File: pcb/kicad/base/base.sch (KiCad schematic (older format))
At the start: 34 parts, among them P1 J-Link SWD, P2 SMA, P3 Power Source, U1 SAMB11G18A-edit, Y1 32.768kHz, Y2 26MHz

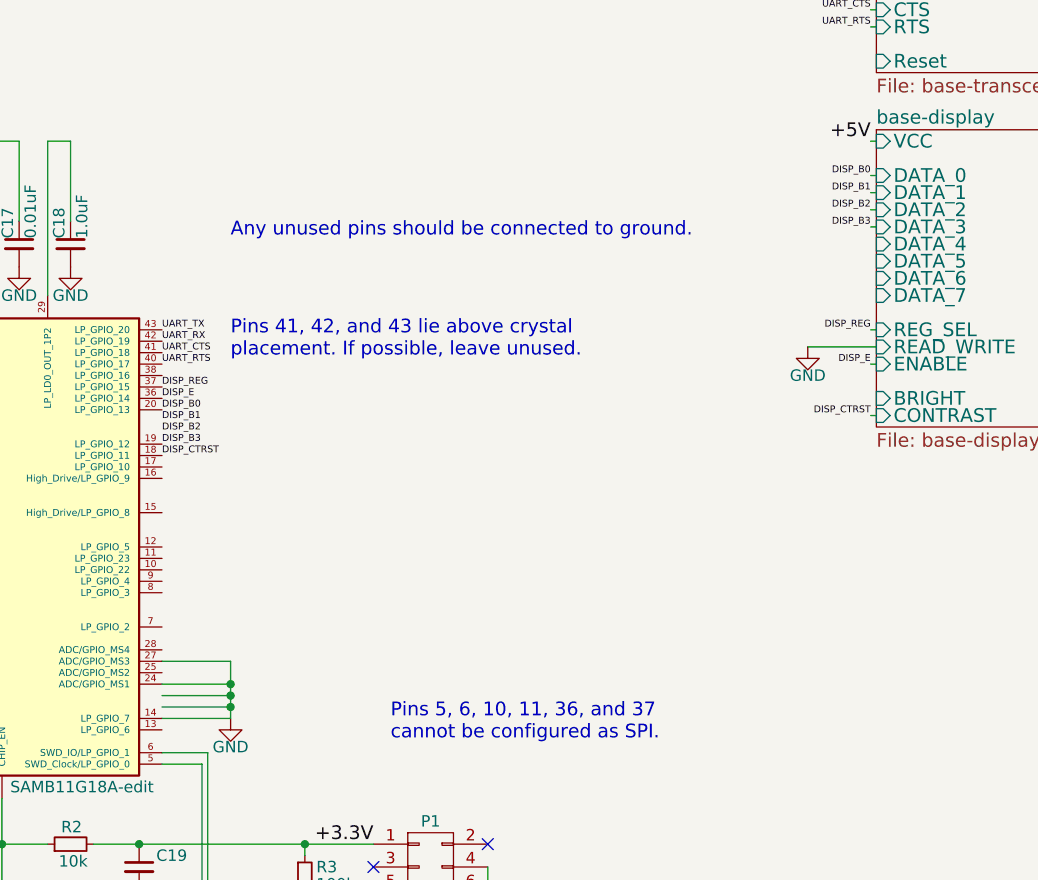
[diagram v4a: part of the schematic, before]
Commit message: Fix power and display routing with proper via size
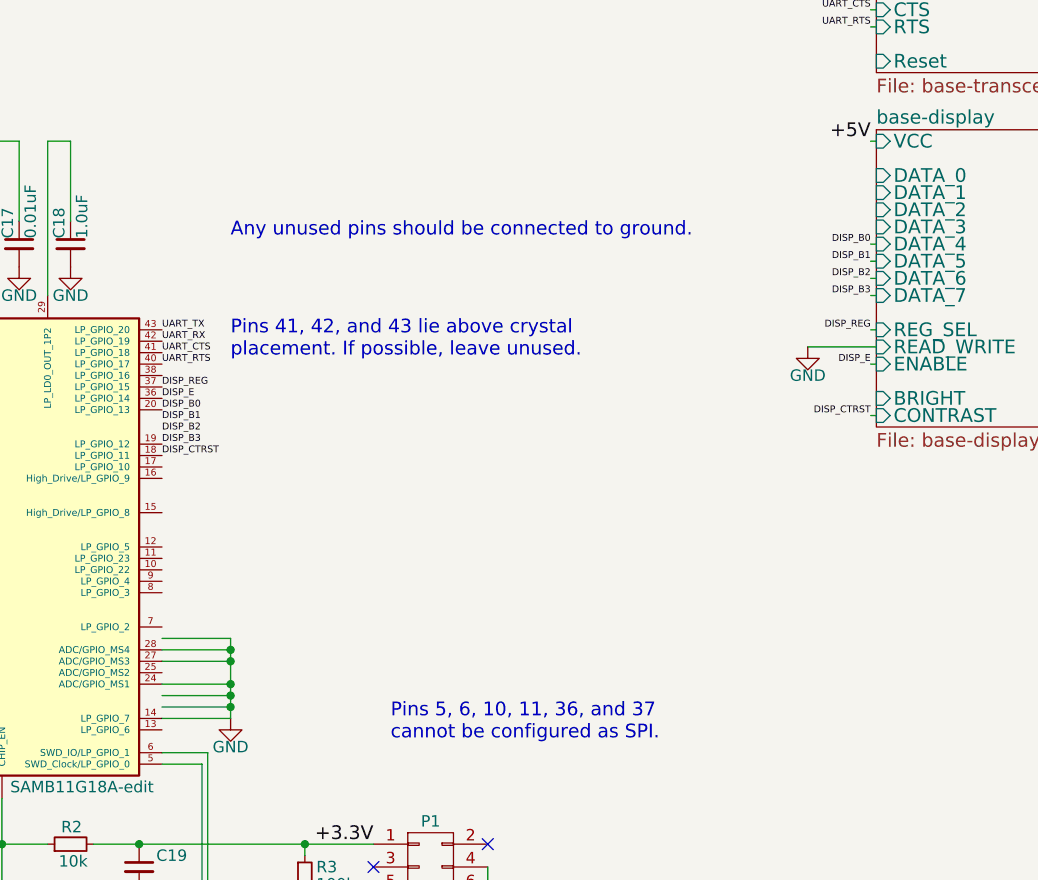
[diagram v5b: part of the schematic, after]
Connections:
- wire segments 97 -> 99
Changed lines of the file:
@@
 	6750 4000 7050 4000
 Wire Wire Line
-	7050 4000 7050 4250
+	7050 3900 7050 4250
 Wire Wire Line
 	7050 4250 6750 4250
@@
 Wire Wire Line
 	9575 2625 9875 2625
-Text Label 9850 2025 2    30   ~ 0
+Text Label 9850 2325 2    30   ~ 0
 DISP_B2
-Text Label 9850 2100 2    30   ~ 0
+Text Label 9850 2400 2    30   ~ 0
 DISP_B3
 Wire Wire Line
-	9850 2100 9875 2100
+	9850 2400 9875 2400
 Wire Wire Line
-	9850 2025 9875 2025
-Text Label 9850 1950 2    30   ~ 0
+	9850 2325 9875 2325
+Text Label 9850 2250 2    30   ~ 0
 DISP_B1
-Text Label 9850 1875 2    30   ~ 0
+Text Label 9850 2175 2    30   ~ 0
 DISP_B0
 Text Label 9850 1725 2    60   ~ 0
@@
 $EndSheet
 Wire Wire Line
-	9850 1950 9875 1950
+	9850 2250 9875 2250
 Wire Wire Line
-	9850 1875 9875 1875
+	9850 2175 9875 2175
 Wire Wire Line
 	9850 1725 9875 1725
+Wire Wire Line
+	6750 3950 7050 3950
+Connection ~ 7050 4000
+Wire Wire Line
+	6750 3900 7050 3900
+Connection ~ 7050 3950
 $EndSCHEMATC

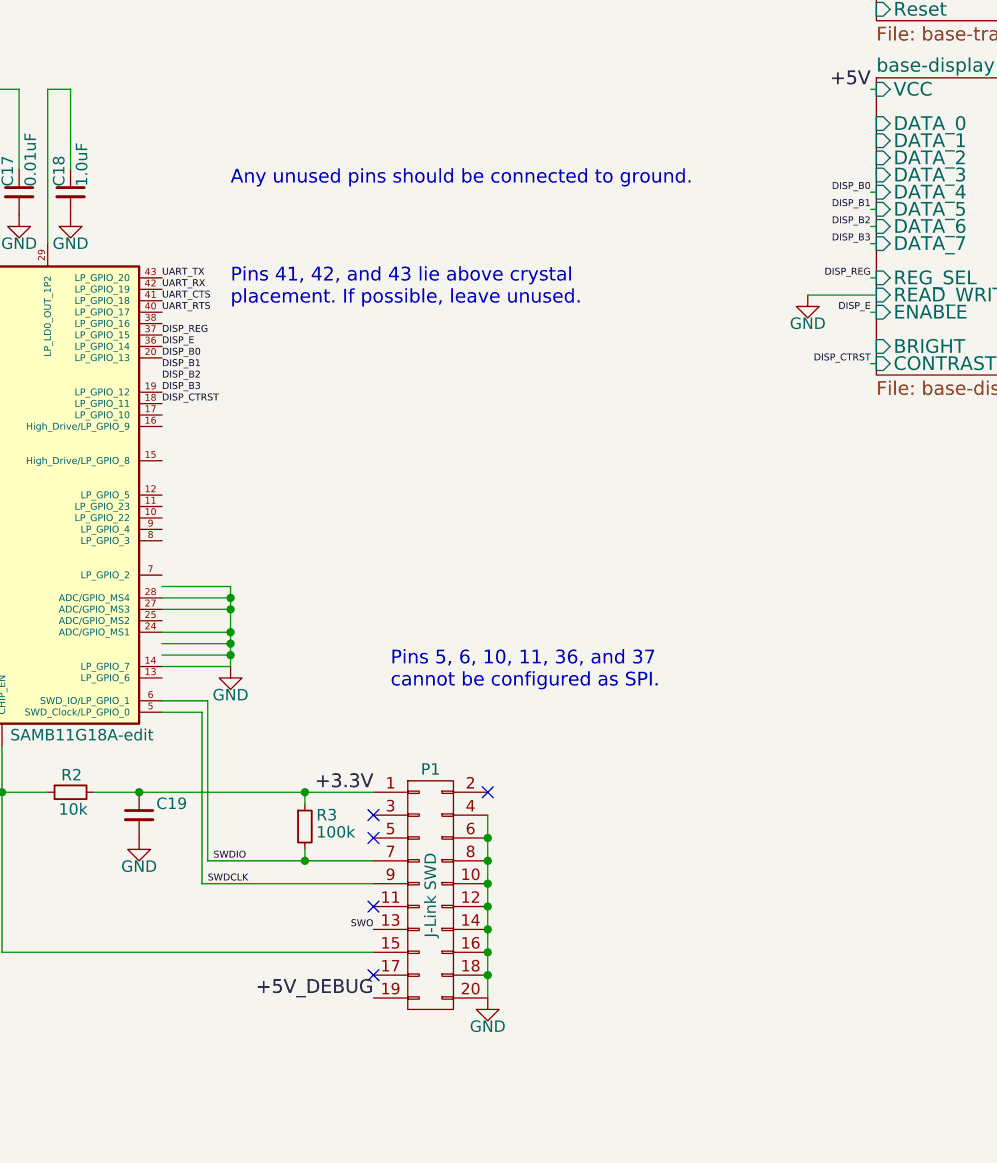
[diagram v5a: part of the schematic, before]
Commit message: Add USB micro B receptacle footprint
USB B footprint generated for potential data/debugging connection.
XBee could potentially move to bottom right corner of layout by using
UART pins near the bottom of the uC (12-20) and moving the display pins
to the top (36-42). Speaker can be placed directly to the above (to the
right in layout) the display.
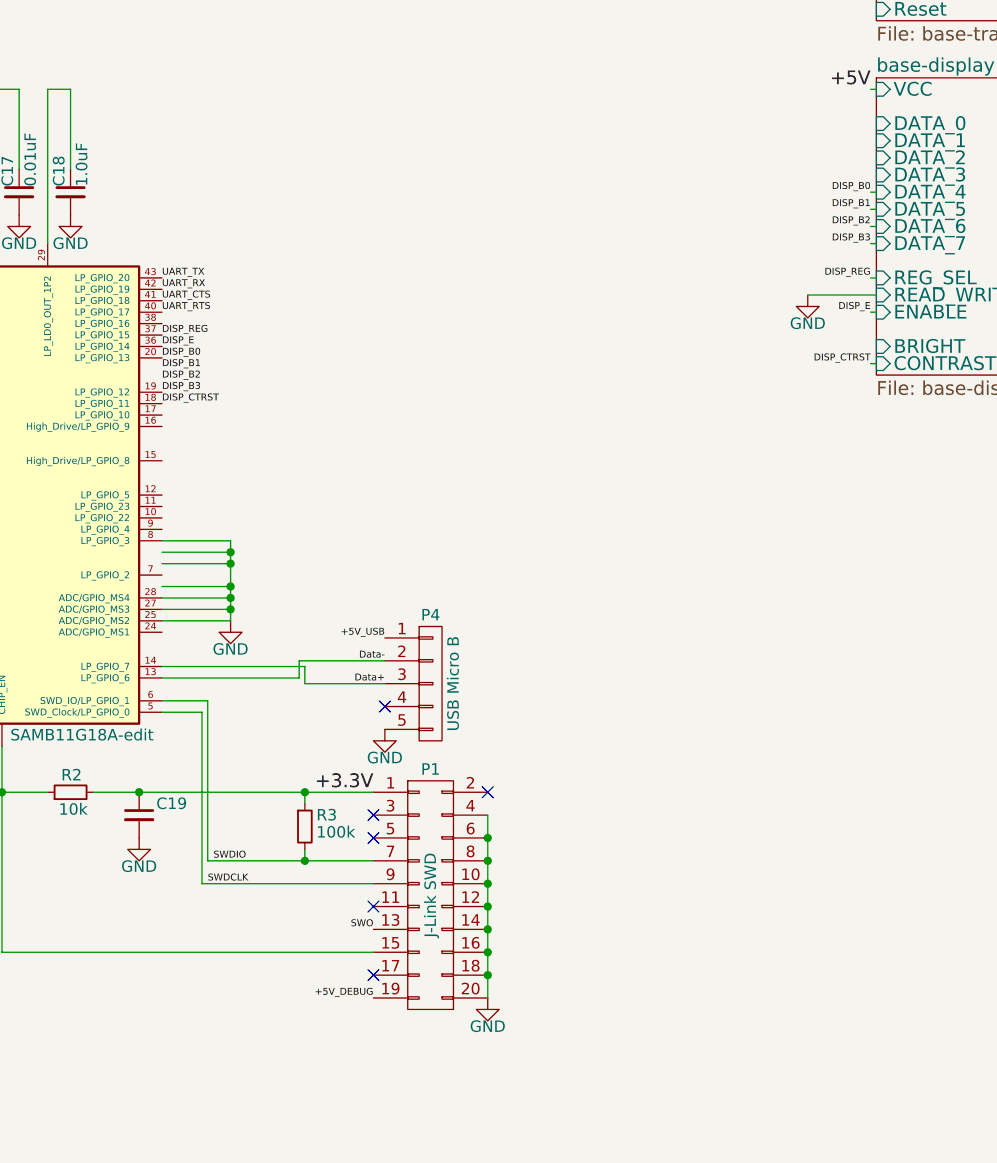
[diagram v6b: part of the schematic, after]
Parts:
- added P4: USB Micro B, Connectors:USB_Micro-B_10118194-000XLF, symbol CONN_01X05
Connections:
- net labels added: +5V_USB, Data+, Data-
- wire segments 99 -> 105
- no-connect marks 9 -> 10
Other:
- note removed: "Any unused pins should be connected to ground."
- note removed: "Pins 41, 42, and 43 lie above crystal\nplacement. If possible, leave unused."
- note removed: "Pins 5, 6, 10, 11, 36, and 37\ncannot be configured as SPI.\n"
